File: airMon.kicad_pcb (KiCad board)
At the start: 2 copper layers, 64.8 x 99.7 mm, 132 parts, among them J1 JTAG, J10 I2C_2_2, J11 I2C_2_3_Buffer, J12 I2C_2_4_Buffer, J13 GPS, J14 A3, J15 A4, J16 Rain, J17 GPIO, J18 Wind, J19 USB_B_Micro, J2 PMS7003, J20 Power, J21 LORA_1, J22 LORA_2, J3 PMSx003, J4 SDS011, J5 Conn_01x05, J6 SW, J7 I2C_1_1, J8 I2C_1_2, J9 I2C_2_1, Q1 2N7002, Q2 AO3401A, Q3 SS8050, Q4 SS8050, Q5 2N7002, Q6 DMP6023LE-13, Q7 2N7002, Q8 DMP6023LE-13, Q9 DMP6023LE-13, SW1 RESET, SW2 Boot, U1 ESP32-WROOM-32, U2 P82B715, U3 L70/L76/MAX-M8C/MAX-M8Q/MAX-8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, U4 PCA9536D, U5 CH340C, U6 LMR14010ADDCR, U7 LMR14010ADDCR, U8 RFM95W-868S2

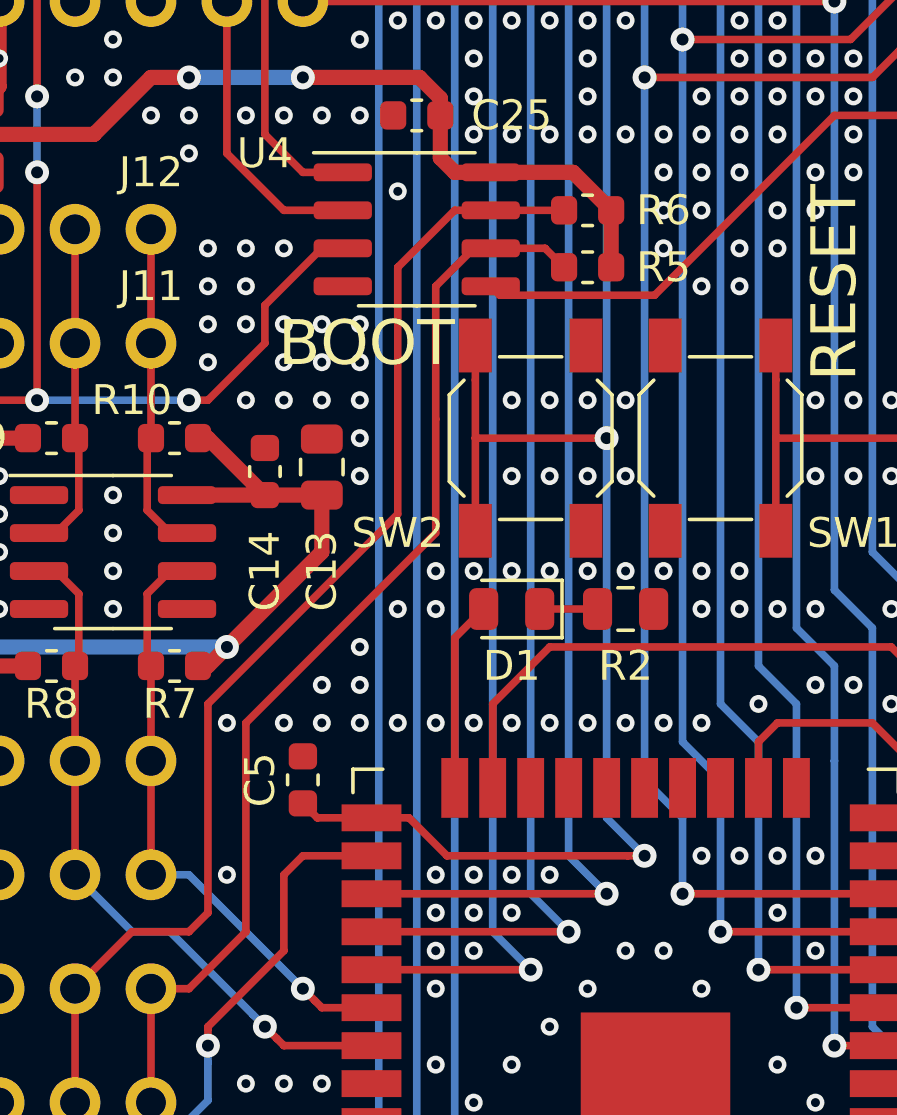
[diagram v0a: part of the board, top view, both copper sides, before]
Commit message: Swaped two wrong I2C signals.
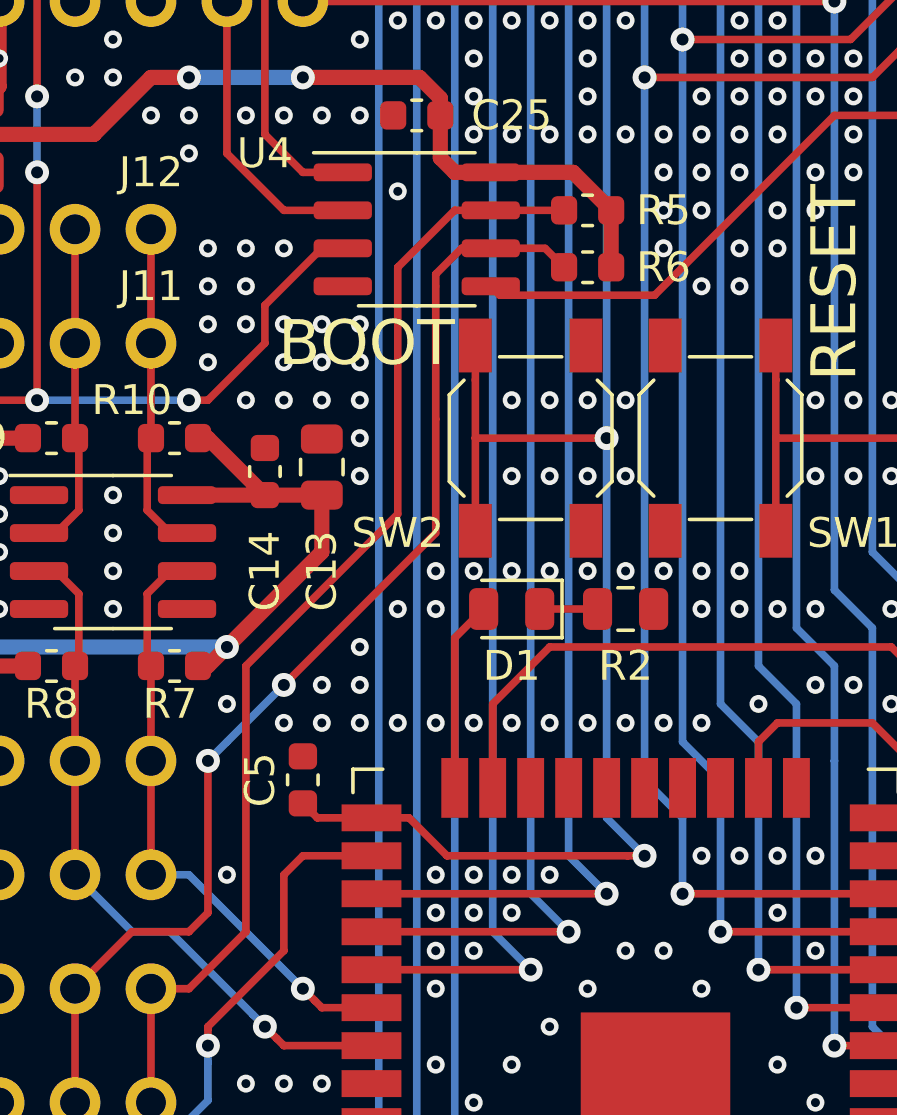
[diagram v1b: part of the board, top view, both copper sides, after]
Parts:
- removed REF**: PMS7003, global:PMS7003
- removed REF**: OSHW-Logo_7.5x8mm_SilkScreen, Symbol:OSHW-Logo_7.5x8mm_SilkScreen
- moved R5 1.91 mm to (50.2, 80.6)
- moved R6 1.91 mm to (50.2, 82.5)
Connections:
- U4 pad 6: /SDA_1 -> /SCL_1
- U4 pad 7: /SCL_1 -> /SDA_1
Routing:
- net /SDA_1: track 44.7 -> 46.3 mm
- net /SCL_1: track 51.6 -> 50.5 mm, vias 0 -> 2
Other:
- board text added: "v0.3"
- board text removed: "v0.2"
